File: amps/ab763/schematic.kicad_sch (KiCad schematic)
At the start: 114 parts, among them T1 125P33A, T2 125C3A, T3 125A1A, T4 125A20B

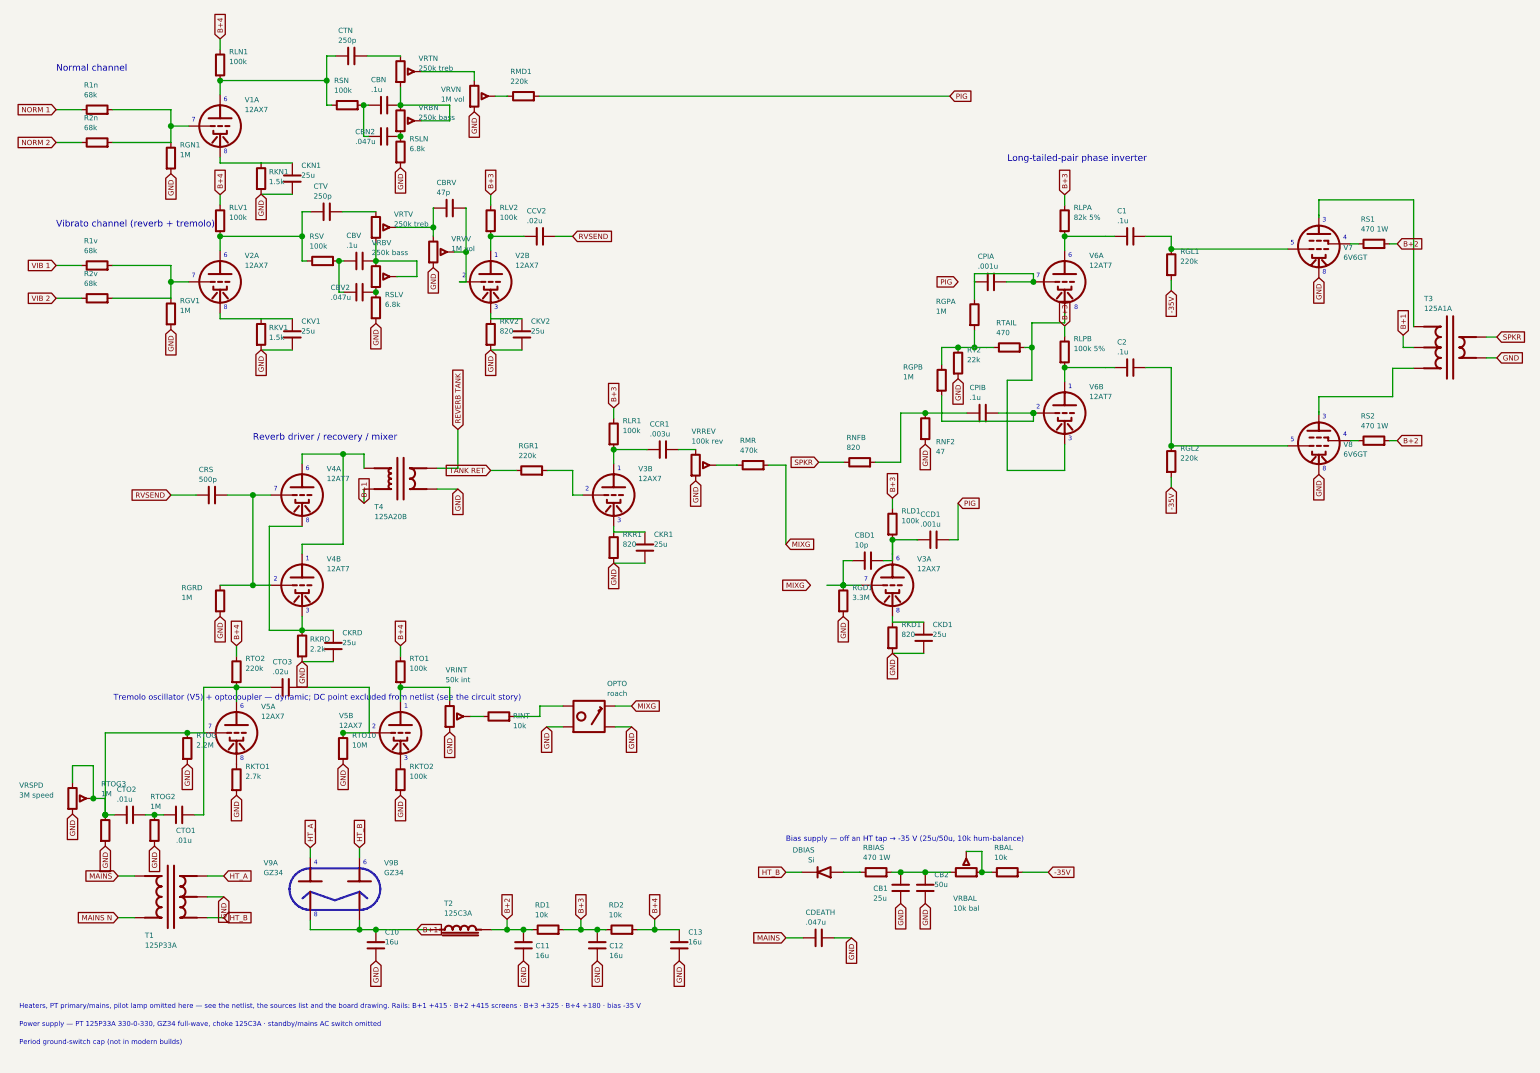
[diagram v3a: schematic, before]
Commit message: Fix: the AB763 sheet drew no Normal second stage, a cathode network the drawing does not have, and four preamp loads on the wrong rail
This sheet claims schematic_claim: verified.

- V1B drawn after the Normal volume. Grid off the wiper (the pot's grounded
  end is the DC return, declared in sch_map.yaml as element_pins RGN2),
  RLN2 100k to B+4, plate -> CCN2 .047u -> RMN2 220k -> PIG. The volume
  wiper used to run through RMD1 220k straight to PIG.
- Boxes [A] and [E] drawn as global labels KA/KE onto the one network each
  box names: RKV2/CKV2 at V2B, now carrying V1B too, and RKR1/CKR1 at V3B,
  now carrying V3A too. V3A's own RKD1/CKD1 are gone.
- RLV2, RLR1 and RLD1 move from B+3 to B+4. B+3 (node [C]) now feeds only
  the phase-inverter plates.
- Mix driver: CCD1 is lettered .1 on the drawing (the sheet said .001u), and
  RMD1 220k sits between it and PIG.
- Valve sections per the factory layout page. On both channel bottles, pin 1
  (the input-stage plate) runs to the tone-stack eyelet, and pin 6 (the
  second-stage plate) runs to the coupler's eyelet. So V1A/V2A are unit 2
  and V1B/V2B unit 1.
- Docstring and title notes: node letters for B+3/B+4 (the chart prints no
  voltage at [D]), plus a KA/KE line.

verify_schematic_nets ab763: PASS (claimed). reference/sheet-board.yaml
re-exported. Sheet vs board now reports V1/V2 section swaps, the [E] split,
RKD1/CKD1 board-only, and RLV2/RLR1/RLD1 misplaced. Those are the board
delta: layout.yaml follows in its own commit.

Co-Authored-By: Claude Opus 5 (1M context) <noreply@anthropic.com>
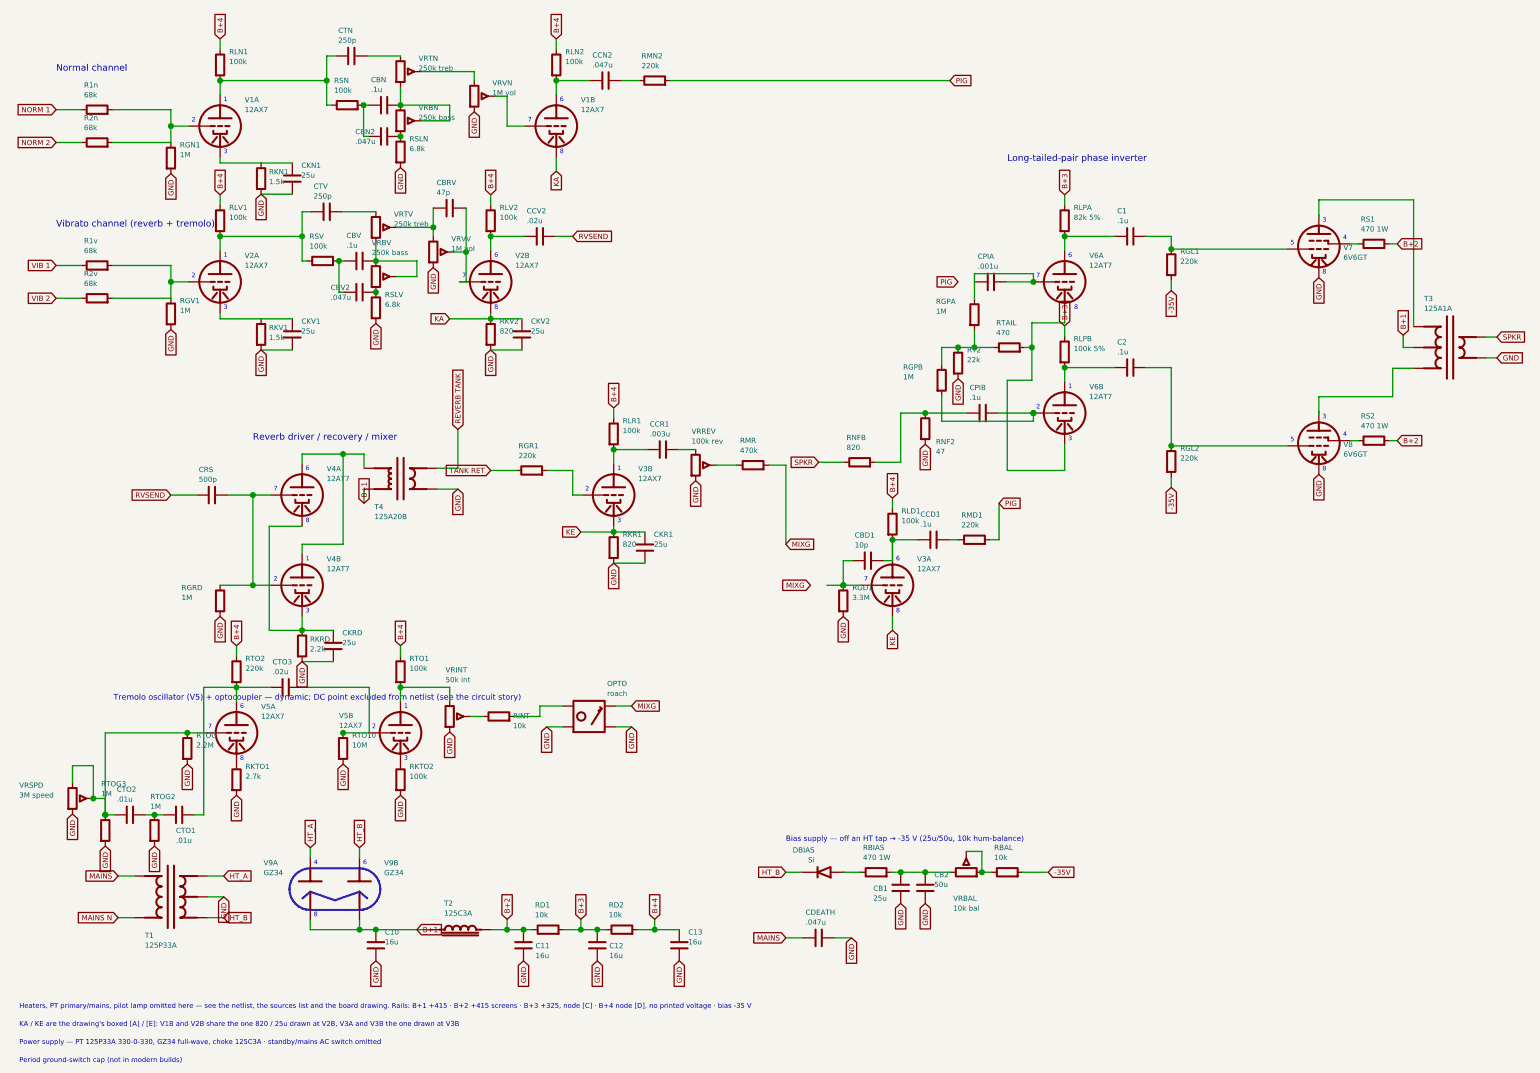
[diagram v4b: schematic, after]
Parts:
- removed C13: 16u, symbol cx:C
- removed CBD1: 10p, symbol cx:C
- removed CBRV: 47p, symbol cx:C
- removed CBV: .1u, symbol cx:C
- removed CKD1: 25u, symbol cx:C
- removed CTO1: .01u, symbol cx:C
- removed DBIAS: Si, symbol cx:DIODE_SS
- removed R1v: 68k, symbol cx:R
- removed RGL1: 220k, symbol cx:R
- removed RKD1: 820, symbol cx:R
- removed RKTO2, RLR1: 100k, symbol cx:R
- removed RTOG: 2.2M, symbol cx:R
- removed T2: 125C3A, symbol cx:CHOKE
- removed V2B, V3B: 12AX7, symbol cx:TRIODE
- removed VRBV: 250k bass, symbol cx:POT
- removed VRINT: 50k int, symbol cx:POT
- added C12: 16u, symbol cx:C
- added CCN2: .047u, symbol cx:C
- added CTO2: .01u, symbol cx:C
- added OPTO: roach, symbol cx:OPTO
- added RBAL: 10k, symbol cx:R
- added RGRD, RTOG2: 1M, symbol cx:R
- added RKV2: 820, symbol cx:R
- added RLN2, RLV1, RLV2: 100k, symbol cx:R
- added RMN2, RTO2: 220k, symbol cx:R
- added RSLV: 6.8k, symbol cx:R
- added RTAIL: 470, symbol cx:R
- added T3: 125A1A, symbol cx:OT_PP
- added V1B: 12AX7, symbol cx:TRIODE
- added VRBAL: 10k bal, symbol cx:POT
- added VRREV: 100k rev, symbol cx:POT
- added VRSPD: 3M speed, symbol cx:POT
- C13: renamed from VRBAL; value 10k bal -> 16u; symbol cx:POT -> cx:C
- CBD1: renamed from CCD1; value .001u -> 10p
- CBRV: renamed from RKV2; value 820 -> 47p; symbol cx:R -> cx:C
- CBV: renamed from RSLV; value 6.8k -> .1u; symbol cx:R -> cx:C
- CCD1: renamed from RKTO1; value 2.7k -> .1u; symbol cx:R -> cx:C
- CCV2: renamed from RGRD; value 1M -> .02u; symbol cx:R -> cx:C
- CTO1: renamed from VRSPD; value 3M speed -> .01u; symbol cx:POT -> cx:C
- DBIAS: renamed from RBAL; value 10k -> Si; symbol cx:R -> cx:DIODE_SS
- R1v: renamed from RLV1; value 100k -> 68k
- RGL1: renamed from T3; value 125A1A -> 220k; symbol cx:OT_PP -> cx:R
- RKTO1: renamed from RTOG2; value 1M -> 2.7k
- RKTO2: renamed from CTO2; value .01u -> 100k; symbol cx:C -> cx:R
- RLD1: renamed from RTO2; value 220k -> 100k
- RLR1: renamed from RMR; value 470k -> 100k
- RMR: renamed from RLD1; value 100k -> 470k
- RTOG: renamed from OPTO; value roach -> 2.2M; symbol cx:OPTO -> cx:R
- T2: renamed from C12; value 16u -> 125C3A; symbol cx:C -> cx:CHOKE
- V1A, V2A: Basing_unit (none) -> 2
- V2B: renamed from CCV2; value .02u -> 12AX7; symbol cx:C -> cx:TRIODE; Basing_unit (none) -> 1
- V3B: renamed from VRREV; value 100k rev -> 12AX7; symbol cx:POT -> cx:TRIODE
- V6A: renamed from RTAIL; value 470 -> 12AT7; symbol cx:R -> cx:TRIODE
- VRBV: renamed from VRVV; value 1M vol -> 250k bass
- VRINT: renamed from V6A; value 12AT7 -> 50k int; symbol cx:TRIODE -> cx:POT
- VRVV: renamed from RLV2; value 100k -> 1M vol; symbol cx:R -> cx:POT
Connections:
- net -35V: now also RGL1.2, RBAL.2; no longer DBIAS.2
- net B+1: now also T2.1, T3.2 (CT); no longer RGL1.2 (CT)
- net B+2: now also T2.2
- net B+3: now also C12.1; no longer RMR.1, T2.1, VRVV.1
- net B+4: now also C13.1, RLR1.1, RLN2.1, RLV1.1, RLV2.1, RTO2.1; no longer R1v.1
- net GND: now also C13.2, RKTO2.2, VRINT.3, VRVV.3, C12.2, OPTO.2 (L2), OPTO.4 (P2), RGRD.2, RKV2.2, RSLV.2, RTOG2.2, T3.5 (SEC_C), VRREV.3, VRSPD.3; no longer CBRV.2, CBV.2, CCD1.2, CCV2.2, CTO1.3, RGL1.5 (SEC_C), RTOG.4 (P2), T2.2, V3B.3, VRBV.3
- net HT_B: now also DBIAS.2 (K)
- net MIXG: now also RMR.2, OPTO.3 (P1); no longer RLR1.2, RTOG.3 (P1)
- net PIG: now also RMN2.2; no longer CBD1.2
- net RVSEND: now also CCV2.2; no longer V2B.2
- net SPKR: now also T3.4 (SEC_H); no longer RGL1.4 (SEC_H)
- net VIB 1: now also R1v.1
- net KE: now reaches CKR1.1, RKR1.1
- net KE: now also V3A.3 (K), V3B.3 (K)
- net at C1.1, RLPA.2: now also V6A.1 (P); no longer VRINT.1 (P)
- net at C1.2, V7.2 (G1): now also RGL1.1
- net at RTO1.2, V5B.1 (P): now also VRINT.1
- net at CRS.2, V4A.2 (G), V4B.2 (G): now also RGRD.1; no longer CCV2.1
- net at V3B.2 (G): now also RGR1.2; no longer RLR1.1
- net at RKTO1.1: now also V5A.3 (K); no longer RKTO2.2
- net at V7.1 (P): now also T3.1 (PRI_A); no longer RGL1.1 (PRI_A)
- net at CTV.1, RSV.1, V2A.1 (P): now also RLV1.2; no longer R1v.2
- net at CBV2.1, RSV.2: now also CBV.1
- net at CBV2.2: now also VRBV.3, RSLV.1; no longer CBV.1
- net at VRTV.3: now also CBV.2, VRBV.1, VRBV.2 (W)
- net at V8.1 (P): now also T3.3 (PRI_B); no longer RGL1.3 (PRI_B)
- net at RBIAS.1: now also DBIAS.1 (A)
- net at CB1.1, CB2.1, RBIAS.2: now also VRBAL.1; no longer C13.1
- net at CPIA.1, CPIA.2, RGPA.1: now also V6A.2 (G); no longer VRINT.2 (G)
- net at R2v.2, RGV1.1, V2A.2 (G): now also R1v.2
- net at V3B.1 (P): now also CCR1.1, RLR1.2; no longer CCR1.2
- net at V2B.1 (P): now also CCV2.1, RLV2.2; no longer VRVV.2
- net at CBRV.1: now also VRTV.2 (W), VRVV.1; no longer CKV2.1
- net at RGD1.1, V3A.2 (G): now also CBD1.1
- net at CTO3.1, V5A.1 (P): now also CTO1.2, RTO2.2; no longer RLD1.2
- net at RGPA.2, RGPB.1, RT2.1: now also RTAIL.1; no longer V6A.1
- net at V5B.3 (K): now also RKTO2.1
- net at CCD1.1: now also CBD1.2, RLD1.2, V3A.1 (P); no longer V5A.3 (K)
- net at VRVN.2 (W): now also V1B.2 (G); no longer RMD1.1
- net at RINT.2: now also OPTO.1 (L1); no longer RTOG.1 (L1)
- net at RINT.1: now also VRINT.2 (W)
- new net: RBAL.1, VRBAL.2 (W), VRBAL.3
- new net: CCN2.1, RLN2.2, V1B.1 (P)
- new net: RTAIL.2, V6A.3 (K), V6B.3 (K)
- new net: CTO1.1, CTO2.2, RTOG2.1
- new net: CCR1.2, VRREV.1
- new net: CCN2.2, RMN2.1
- new net: CBRV.2, V2B.2 (G), VRVV.2 (W)
- new net: CCD1.2, RMD1.1
- new net: RMR.1, VRREV.2 (W)
- new net: CTO2.1, RTOG.1, RTOG3.1, V5A.2 (G), VRSPD.1, VRSPD.2 (W)
- new net KA: CKV2.1, RKV2.1, V1B.3 (K), V2B.3 (K)
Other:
- note added: "Heaters, PT primary/mains, pilot lamp omitted here — see the netlist, the sources list and the board drawing. Rails: B+1 +415 · B+2 +415 screens · B+3 +325, node [C] · B+4 node [D], no printed voltage · bias -35 V"
- note added: "KA / KE are the drawing's boxed [A] / [E]: V1B and V2B share the one 820 / 25u drawn at V2B, V3A and V3B the one drawn at V3B"
- note removed: "Heaters, PT primary/mains, pilot lamp omitted here — see the netlist, the sources list and the board drawing. Rails: B+1 +415 · B+2 +415 screens · B+3 +325 · B+4 +180 · bias -35 V"
- moved on the sheet: CBD1, R1v, RKTO1, RLD1, RLR1, RMR, VRBV

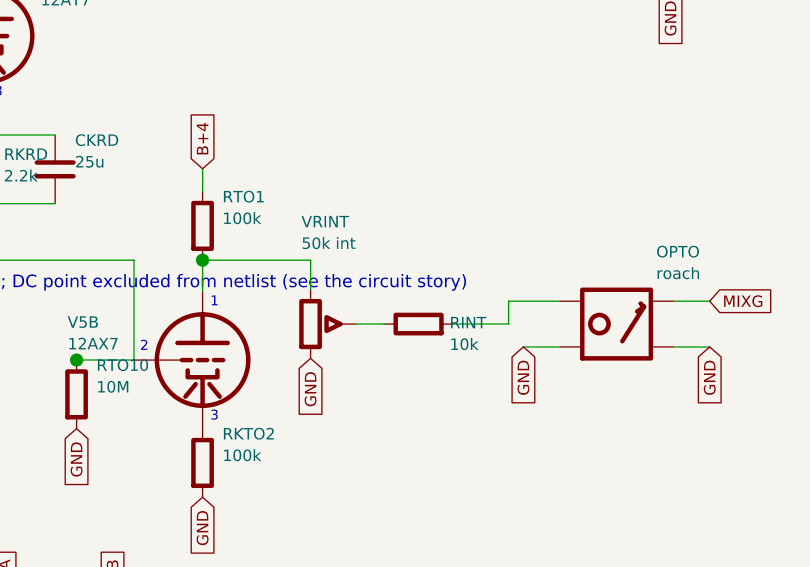
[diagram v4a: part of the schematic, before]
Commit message: Fix: the AB763 parts list and sheet carried a 10k intensity resistor the drawing does not have
RINT (10 kΩ, "tremolo intensity series") appears on neither C-FD page. The
schematic's "10K" beside the 50K-RA INTENSITY control is the bias control's
fixed leg: it runs from the 10K-L pot's end to ground. The layout letters
that resistor inside the 10K-L outline (RBAL, already listed). Removed from
bom.yaml and the sheet. The board never placed it.

Co-Authored-By: Claude Opus 5 (1M context) <noreply@anthropic.com>
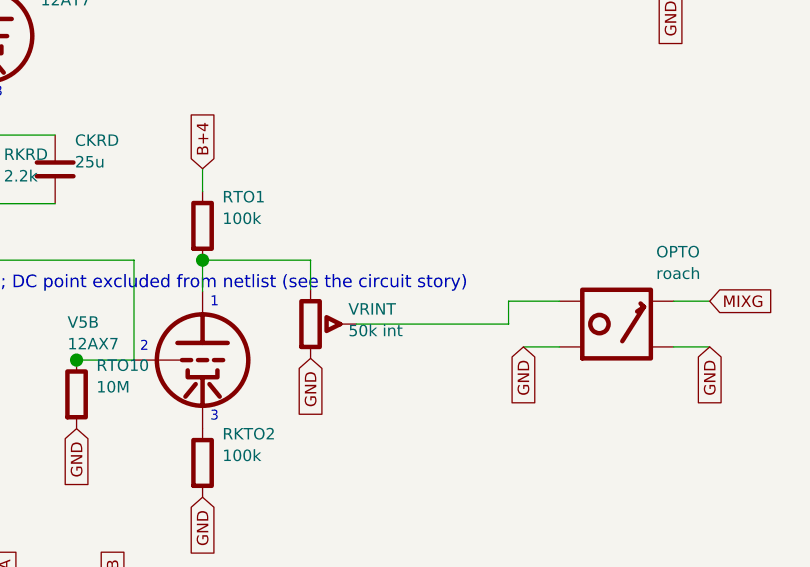
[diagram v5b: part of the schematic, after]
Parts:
- removed RD1, RD2, RINT: 10k, symbol cx:R
- removed RGL1, RGL2: 220k, symbol cx:R
- removed RGPA: 1M, symbol cx:R
- removed RLPA: 82k 5%, symbol cx:R
- added C11, C12: 16u, symbol cx:C
- added RT2: 22k, symbol cx:R
- added V6B: 12AT7, symbol cx:TRIODE
- added V7, V8: 6V6GT, symbol cx:PENTODE
- RD1: renamed from C11; value 16u -> 10k; symbol cx:C -> cx:R
- RD2: renamed from C12; value 16u -> 10k; symbol cx:C -> cx:R
- RGL1: renamed from V7; value 6V6GT -> 220k; symbol cx:PENTODE -> cx:R
- RGL2: renamed from V8; value 6V6GT -> 220k; symbol cx:PENTODE -> cx:R
- RGPA: renamed from RT2; value 22k -> 1M
- RLPA: renamed from V6B; value 12AT7 -> 82k 5%; symbol cx:TRIODE -> cx:R
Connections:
- net -35V: now also RGL1.2, RGL2.2
- net B+2: now also C11.1
- net B+3: now also RD1.2, RLPA.1, C12.1
- net B+4: now also RD2.2
- net GND: now also C11.2, C12.2, RT2.2, V7.4 (K), V8.4 (K); no longer RD1.2, RD2.2, RGL1.4 (K), RGL2.4 (K), RGPA.2
- net at C2.1, RLPB.2: now also V6B.1 (P); no longer RLPA.1 (P)
- net at CPIB.2, RGPB.2: now also V6B.2 (G); no longer RLPA.2 (G)
- net at RTAIL.2, V6A.3 (K): now also V6B.3 (K); no longer RLPA.3 (K)
- net at C1.2: now also RGL1.1, V7.2 (G1); no longer RGL1.2 (G1)
- net at VRINT.2 (W): now also OPTO.1 (L1)
- net at RS1.1: now also V7.3 (G2); no longer RGL1.3 (G2)
- net at T3.3 (PRI_B): now also V8.1 (P); no longer RGL2.1 (P)
- net at C2.2: now also RGL2.1, V8.2 (G1); no longer RGL2.2 (G1)
- net at RS2.1: now also V8.3 (G2); no longer RGL2.3 (G2)
- net at CPIA.1, CPIA.2, V6A.2 (G): now also RGPA.1
- net at RGPB.1, RTAIL.1: now also RGPA.2, RT2.1; no longer RGPA.1
- net at T3.1 (PRI_A): now also V7.1 (P); no longer RGL1.1 (P)
- net at C1.1, V6A.1 (P): now also RLPA.2
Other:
- moved on the sheet: RGPA
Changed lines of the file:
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@@
   (symbol (lib_id "cx:POT") (at 117.7 182.278 0) (unit 1)
     (in_bom yes) (on_board yes)
-    (property "Reference" "VRINT" (at 116.684 170.938 0) (effects (font (size 1.27 1.27)) (justify left)))
-    (property "Value" "50k int" (at 116.684 173.338 0) (effects (font (size 1.27 1.27)) (justify left))))
+    (property "Reference" "VRINT" (at 121.902 180.638 0) (effects (font (size 1.27 1.27)) (justify left)))
+    (property "Value" "50k int" (at 121.902 183.038 0) (effects (font (size 1.27 1.27)) (justify left))))
   (global_label "GND" (shape input) (at 117.7 186.088 270)
     (effects (font (size 1.27 1.27)) (justify right)))
-  (symbol (lib_id "cx:R") (at 129.7 182.278 90) (unit 1)
-    (in_bom yes) (on_board yes)
-    (property "Reference" "RINT" (at 133.14 182.162 270) (effects (font (size 1.27 1.27)) (justify left)))
-    (property "Value" "10k" (at 133.14 184.562 270) (effects (font (size 1.27 1.27)) (justify left))))
-  (wire (pts (xy 122.78 182.278) (xy 125.89 182.278))
-    (stroke (width 0) (type default)))
-  (wire (pts (xy 133.51 182.278) (xy 139.7 182.278))
+  (wire (pts (xy 122.78 182.278) (xy 139.7 182.278))
     (stroke (width 0) (type default)))
   (symbol (lib_id "cx:OPTO") (at 151.7 182.278 0) (unit 1)

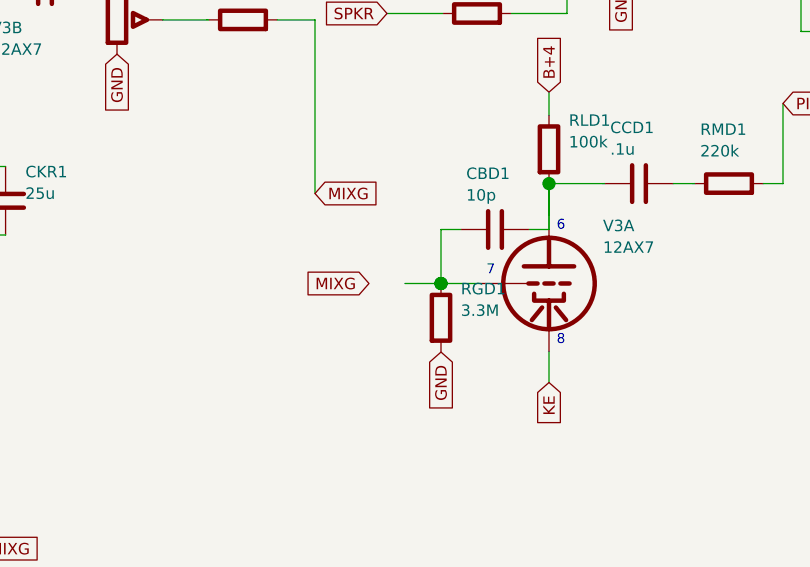
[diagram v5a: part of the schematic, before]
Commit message: Fix: the AB763 sheet's reverb mix and photocell never reached the mix driver's grid
The sheet lettered the node MIXG, but placed the label at the mix driver 4 mm
short of the grid lead (label at x=196, wire from x=200). RMR (the 470k from
the Reverb wiper) and the photocell therefore drew on a net of their own, and
the grid on another. No netlist gate sees this, because both parts sit in the
abstracted mix network. It surfaced when the board wired RMR to the grid, as
the C-FD layout does, and the sheet↔board check called RMR misplaced. The
lead now reaches the label.

Co-Authored-By: Claude Opus 5 (1M context) <noreply@anthropic.com>
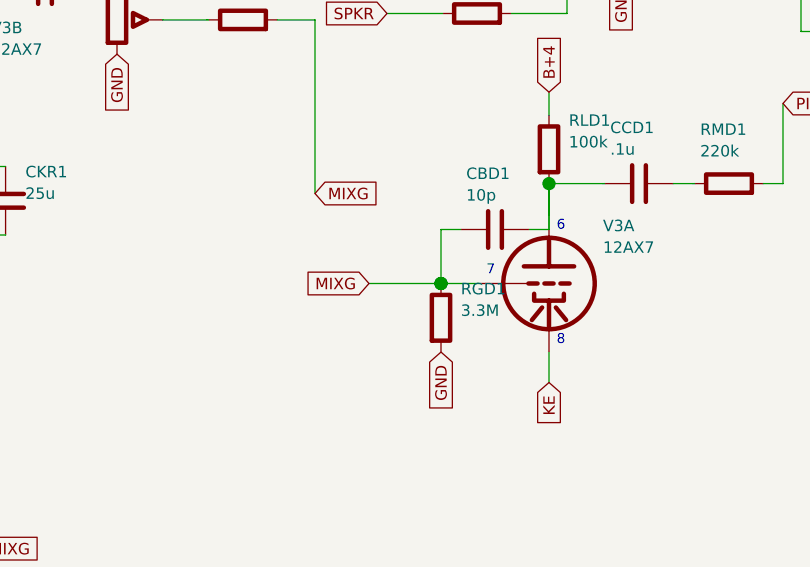
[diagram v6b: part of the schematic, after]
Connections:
- net MIXG: now also CBD1.1, RGD1.1, V3A.2 (G)
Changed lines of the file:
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@@
   (global_label "MIXG" (shape input) (at 205.7 150.278 180)
     (effects (font (size 1.27 1.27)) (justify right)))
-  (wire (pts (xy 209.7 150.278) (xy 213.7 150.278))
+  (wire (pts (xy 205.7 150.278) (xy 213.7 150.278))
     (stroke (width 0) (type default)))
   (junction (at 213.7 150.278) (diameter 1.467) (color 0 0 0 0))
